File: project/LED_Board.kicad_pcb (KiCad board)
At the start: 2 copper layers, 40 x 42 mm, 11 parts, among them J4 Conn_01x02_Male, J5 Conn_01x02_Male, J6 Conn_01x02_Male, J7 Conn_01x02_Male

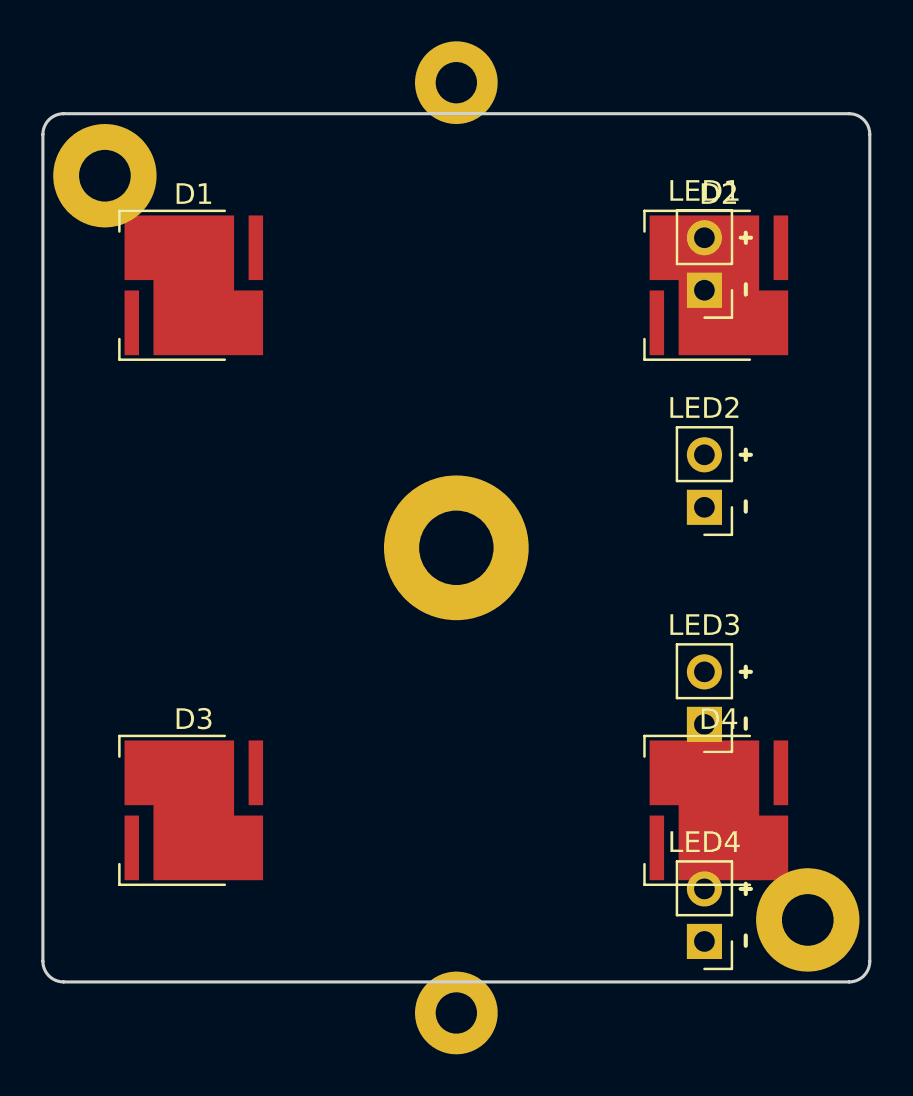
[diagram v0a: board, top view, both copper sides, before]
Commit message: Завершена трассировка платы
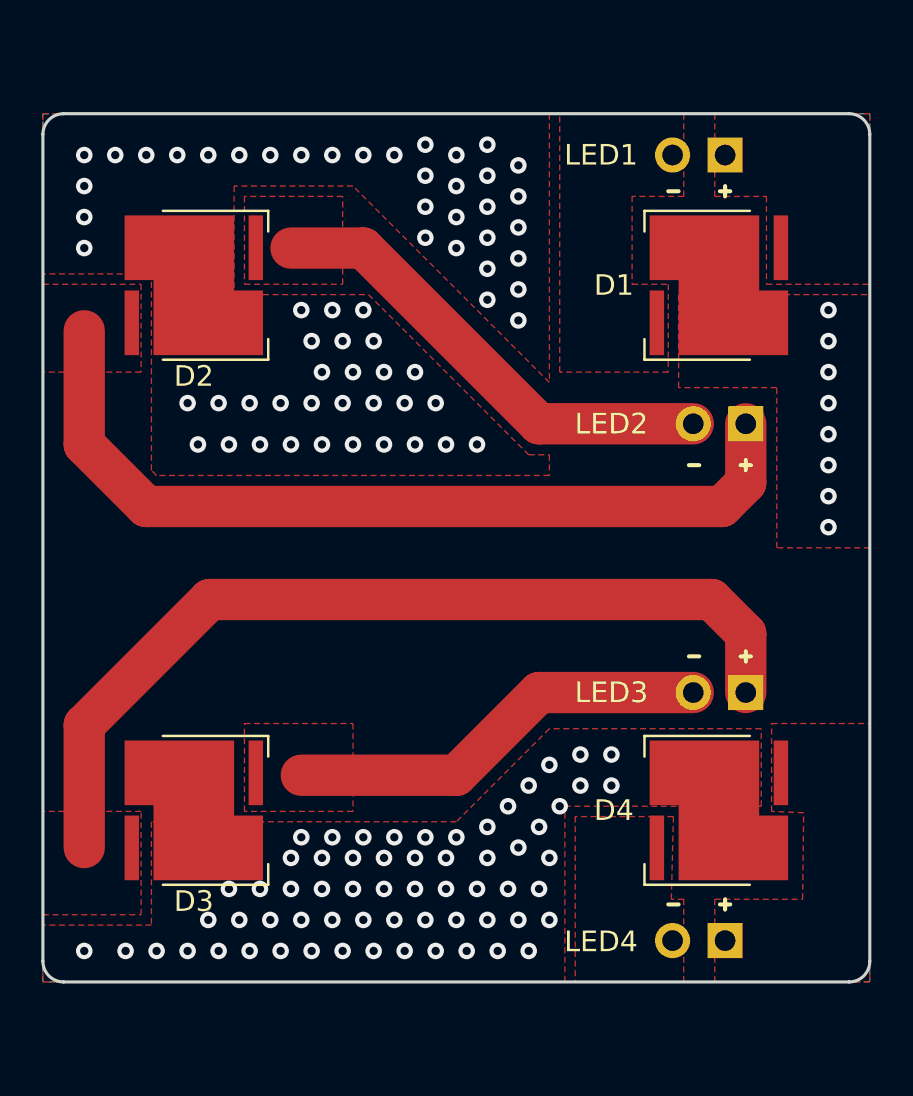
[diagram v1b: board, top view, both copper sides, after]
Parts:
- removed Lens1: Lens, my_lib:Lens_C12361_HB-2X2-W
- removed REF** (x2): MountingHole_2.5mm_Pad, MountingHole:MountingHole_2.5mm_Pad
- J4, J5, J6, J7: moved to B.Cu
- moved D1 25.4 mm to (132.2, 59.3)
- moved D2 25.4 mm to (106.8, 59.3), turned to 180 degrees
- moved J4 6.62 mm to (132.5, 53.0), turned to 90 degrees
- moved J5 4.51 mm to (133.5, 66.0), turned to 90 degrees
- moved J6 2.52 mm to (133.5, 79.0), turned to 90 degrees
- moved J7 1.00 mm to (132.5, 91.0), turned to 90 degrees
- turned D3 to 180 degrees
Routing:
- net /LED3+: track 0.00 -> 44.0 mm
- net /LED2+: track 0.00 -> 42.1 mm
- net /T: track 0.00 -> 35.4 mm, vias 0 -> 134
- net /LED2-: track 0.00 -> 23.0 mm
- net /LED3-: track 0.00 -> 20.6 mm
- added copper zone on F.Cu, net /LED1+
- added copper zone on F.Cu, net /LED1-
- added copper zone on F.Cu, net /LED2+
- added copper zone on F.Cu, net /LED2-
- added copper zone on F.Cu, net /LED3+
- added copper zone on F.Cu, net /LED3-
- added copper zone on F.Cu, net /LED4+
- added copper zone on F.Cu, net /LED4-
- added copper zone on B.Cu, net /T
- added copper zone on F.Cu, net /T
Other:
- net class POWER removed
